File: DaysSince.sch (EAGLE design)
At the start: 3 parts

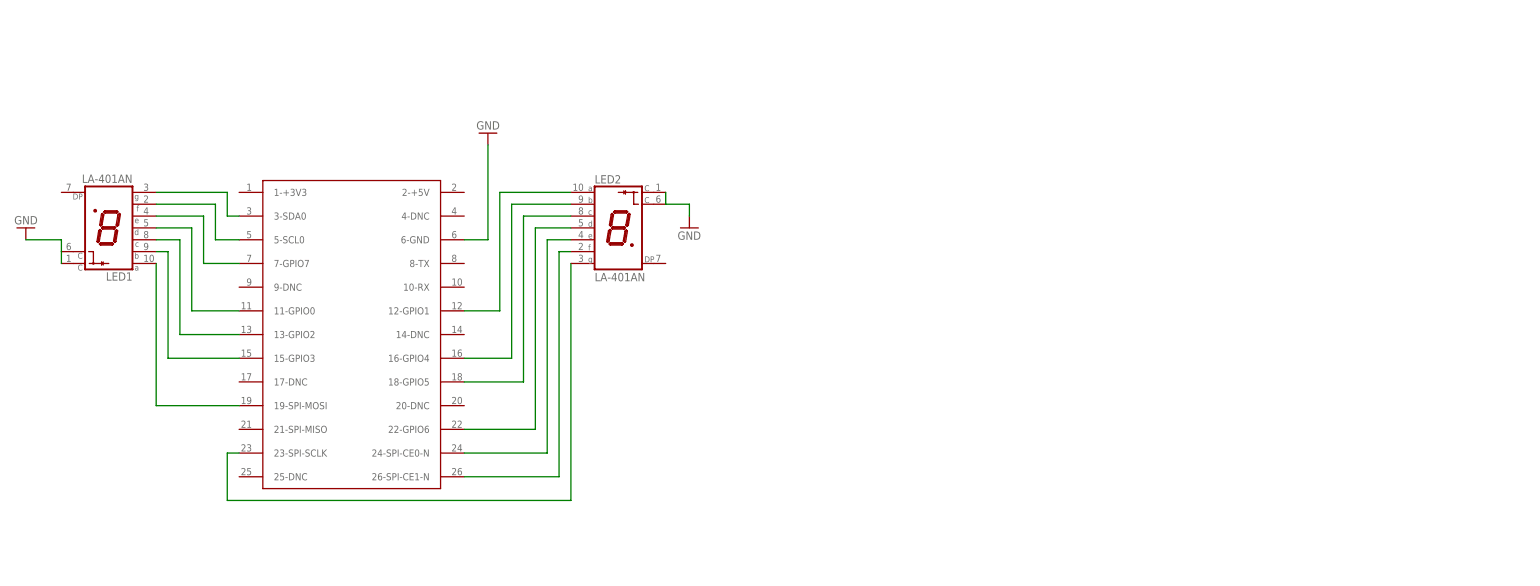
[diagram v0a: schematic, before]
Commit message: New and improved version
Smaller PCB, shift registers, and lower cost, woo.
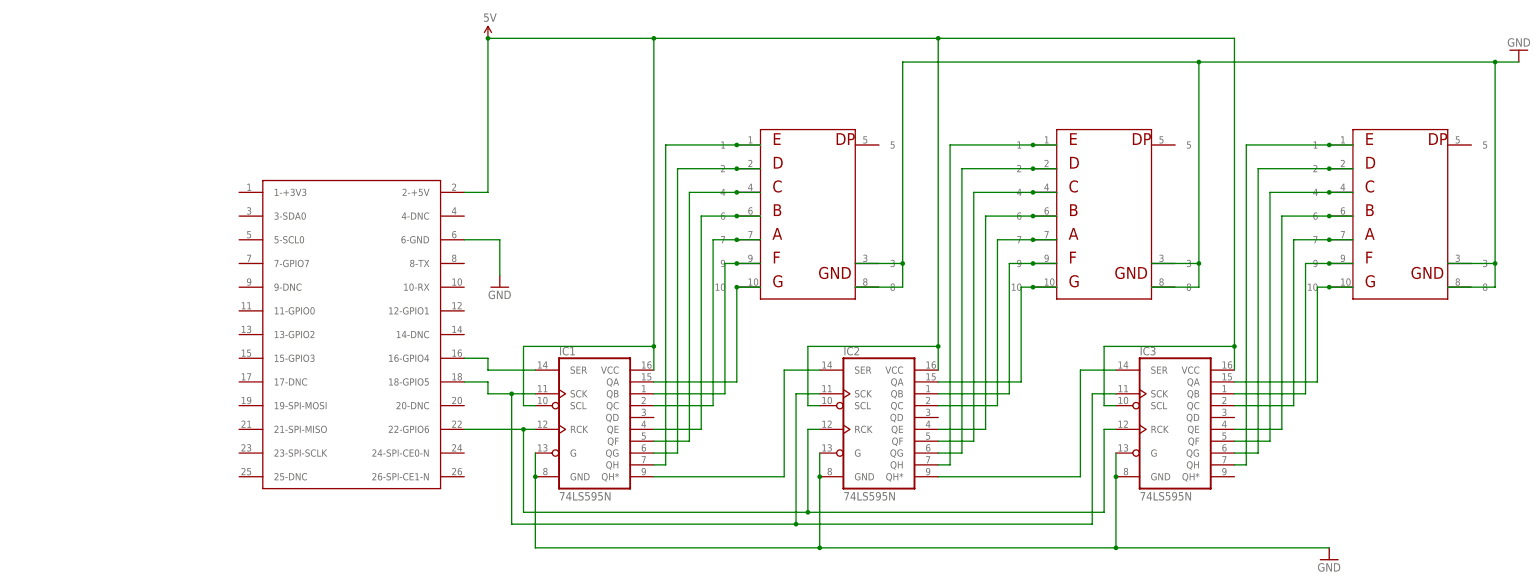
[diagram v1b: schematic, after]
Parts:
- added IC1, IC2, IC3: 74LS595N, SparkFun-DigitalIC:74LS595N
- added LED3: 7SG100012AG, Benchoff:7SG100012AG
- LED1, LED2: value LA-401AN -> 7SG100012AG; device led-7-segment:LA-401AN -> Benchoff:7SG100012AG
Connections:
- new net 5V: IC1.SCL, IC1.VCC, IC2.SCL, IC2.VCC, IC3.SCL, IC3.VCC, U$1.2-+5V
- new net N$1: IC1.QH*, IC2.SER
- new net N$10: IC1.QG, LED1.2
- new net N$17: IC2.QG, LED2.2
- new net N$18: IC2.QF, LED2.4
- new net N$19: IC2.QA, LED2.10
- new net N$20: IC3.QH, LED3.1
- new net N$21: IC3.QG, LED3.2
- new net N$22: IC3.QF, LED3.4
- new net N$23: IC3.QE, LED3.6
- new net N$24: IC3.QC, LED3.7
- new net N$25: IC3.QB, LED3.9
- new net N$26: IC3.QA, LED3.10
- net GND: now also IC1.G, IC1.GND, IC2.G, IC2.GND, IC3.G, IC3.GND, LED1.3, LED1.8, LED2.3, LED2.8, LED3.3, LED3.8; no longer LED1.C@1, LED1.C@2, LED2.C@1, LED2.C@2
- net N$11: now also IC1.QF, LED1.4; no longer LED2.B, U$1.16-GPIO4
- net N$12: now also IC1.QE, LED1.6; no longer LED2.C, U$1.18-GPIO5
- net N$13: now also IC1.QC, LED1.7; no longer LED2.D, U$1.22-GPIO6
- net N$14: now also IC1.QB, LED1.9; no longer LED2.E, U$1.24-SPI-CE0-N
- net N$15: now also IC1.QA, LED1.10; no longer LED2.F, U$1.26-SPI-CE1-N
- net N$16: now also IC2.QH, LED2.1; no longer LED2.G, U$1.23-SPI-SCLK
- net N$2: now also IC2.QH*, IC3.SER; no longer LED1.G, U$1.3-SDA0
- net N$3: now also IC2.QE, LED2.6; no longer LED2.A, U$1.12-GPIO1
- net N$4: now also IC1.RCK, IC2.RCK, IC3.RCK, U$1.22-GPIO6; no longer LED1.F, U$1.5-SCL0
- net N$5: now also IC1.SCK, IC2.SCK, IC3.SCK, U$1.18-GPIO5; no longer LED1.E, U$1.7-GPIO7
- net N$6: now also IC1.SER, U$1.16-GPIO4; no longer LED1.D, U$1.11-GPIO0
- net N$7: now also IC2.QC, LED2.7; no longer LED1.C, U$1.13-GPIO2
- net N$8: now also IC2.QB, LED2.9; no longer LED1.B, U$1.15-GPIO3
- net N$9: now also IC1.QH, LED1.1; no longer LED1.A, U$1.19-SPI-MOSI
